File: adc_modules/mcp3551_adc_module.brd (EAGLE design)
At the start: 100 x 80 mm, 0 parts

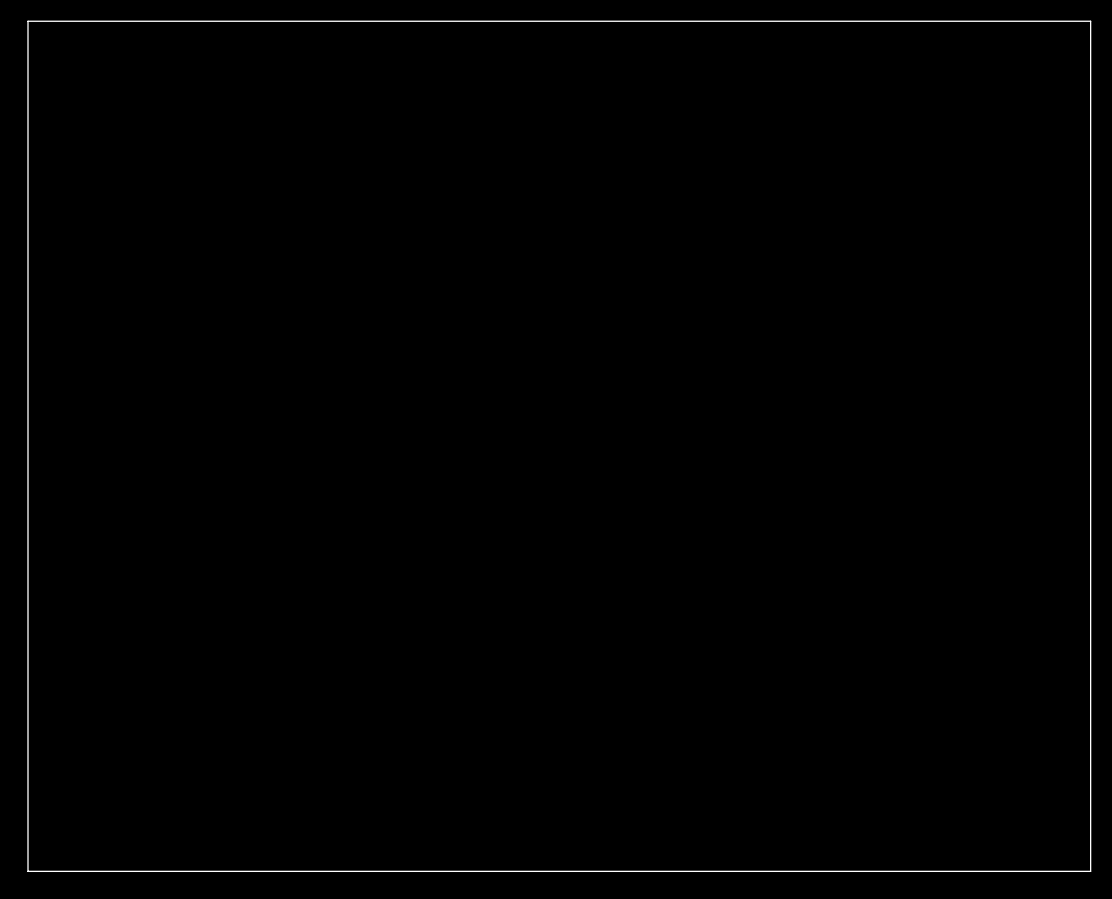
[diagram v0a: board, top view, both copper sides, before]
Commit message: * updated and almost finished MCP3551 ADC module
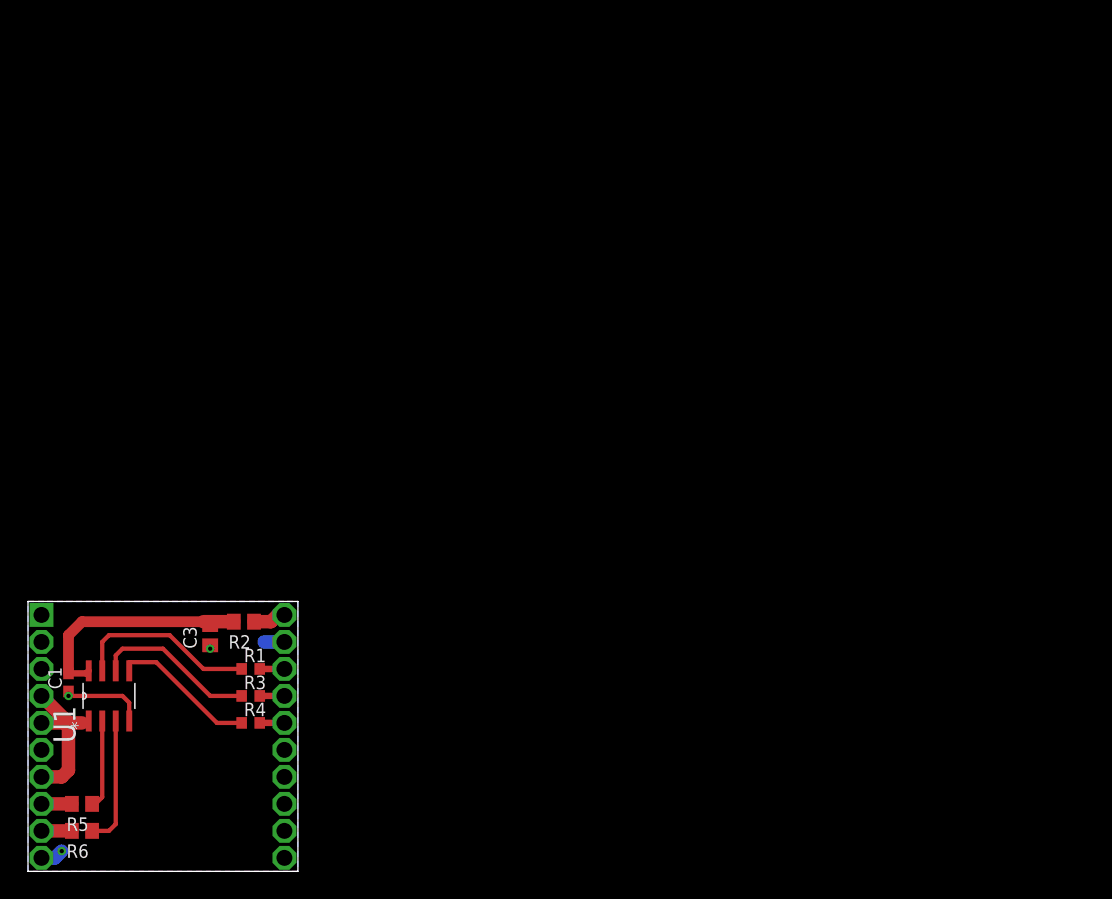
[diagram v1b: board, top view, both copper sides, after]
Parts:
- added C1: 100n, SquantorRCL:C0603
- added C3: 10u, SquantorRCL:C0805
- added R1, R3, R4: 100, SquantorRCL:R0603
- added R2: ferrite, SquantorRCL:R0805
- added R5, R6: 5.1k, SquantorRCL:R0805
- added U$1: METROLOGY_MODULE1.5MM, SquantorPCBOutline:METROLOGY_MODULE_1.5MM_HOLE
- added U1: MCP3553-E/SN, SquantorMicrochip:SOIC127P600X175-8N
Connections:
- new net ADC_CS: R1.1, U1.7
- new net ADC_SCK: R4.1, U1.5
- new net ADC_SDO: R3.1, U1.6
- new net ADC_VIN+: R5.1, U1.2
- new net ADC_VIN-: R6.1, U1.3
- new net GND: C1.1, C3.1, U$1.P$10, U$1.P$19, U$1.P$6, U1.4
- new net N$1: R2.1, U$1.P$20
- new net N$2: R1.2, U$1.P$18
- new net N$3: R3.2, U$1.P$17
- new net N$4: R4.2, U$1.P$16
- new net N$5: R5.2, U$1.P$8
- new net N$6: R6.2, U$1.P$9
- new net VCC: C1.2, C3.2, R2.2, U1.8
- new net VREF: U$1.P$4, U$1.P$5, U$1.P$7, U1.1
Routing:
- net VCC: track 0.00 -> 22.0 mm
- net ADC_CS: track 0.00 -> 17.4 mm
- net ADC_SDO: track 0.00 -> 15.4 mm
- net VREF: track 0.00 -> 15.4 mm
- net ADC_SCK: track 0.00 -> 13.8 mm
- net GND: track 0.00 -> 12.5 mm, vias 0 -> 3
- net ADC_VIN-: track 0.00 -> 12.2 mm
- net ADC_VIN+: track 0.00 -> 8.38 mm
- net N$1: track 0.00 -> 3.12 mm
- net N$6: track 0.00 -> 2.86 mm
- net N$5: track 0.00 -> 2.86 mm
- net N$4: track 0.00 -> 2.32 mm
- net N$3: track 0.00 -> 2.32 mm
- net N$2: track 0.00 -> 2.32 mm
- added copper zone on layer 16, net GND
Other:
- board size 100 x 80 mm -> 25.4 x 25.4 mm

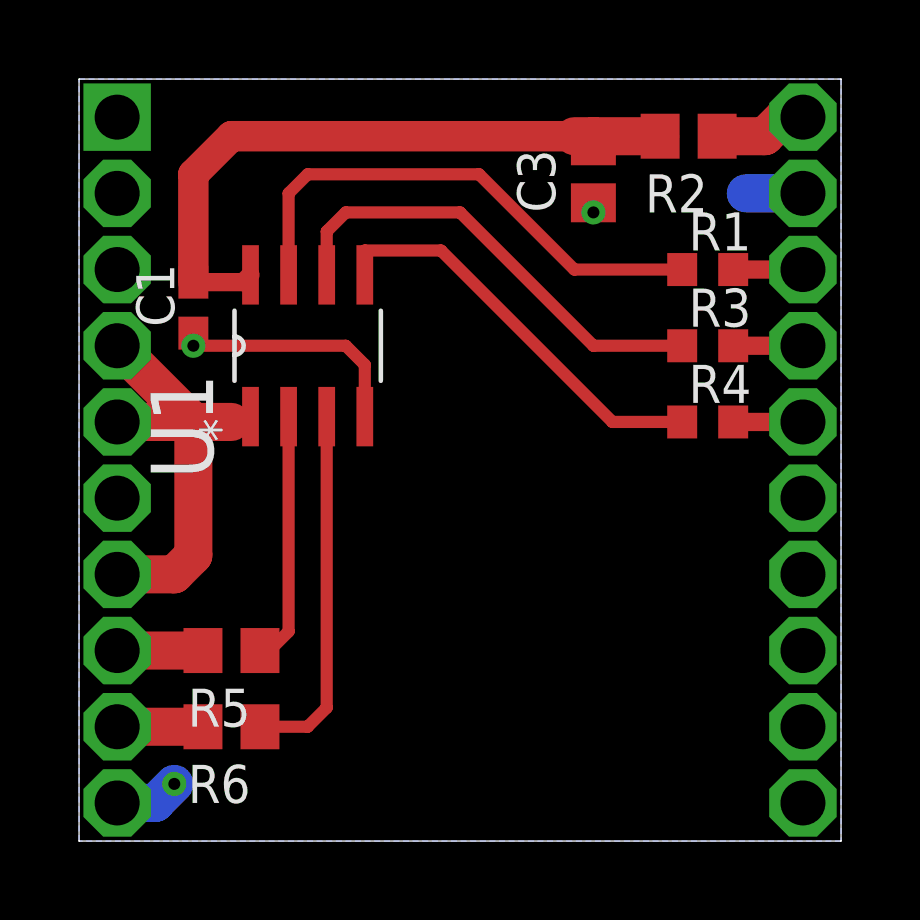
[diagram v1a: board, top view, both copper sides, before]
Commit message: * updated board format * made the LTC6655 reference module more compact, hopefully better * small modifications to the MCP355X ADC module
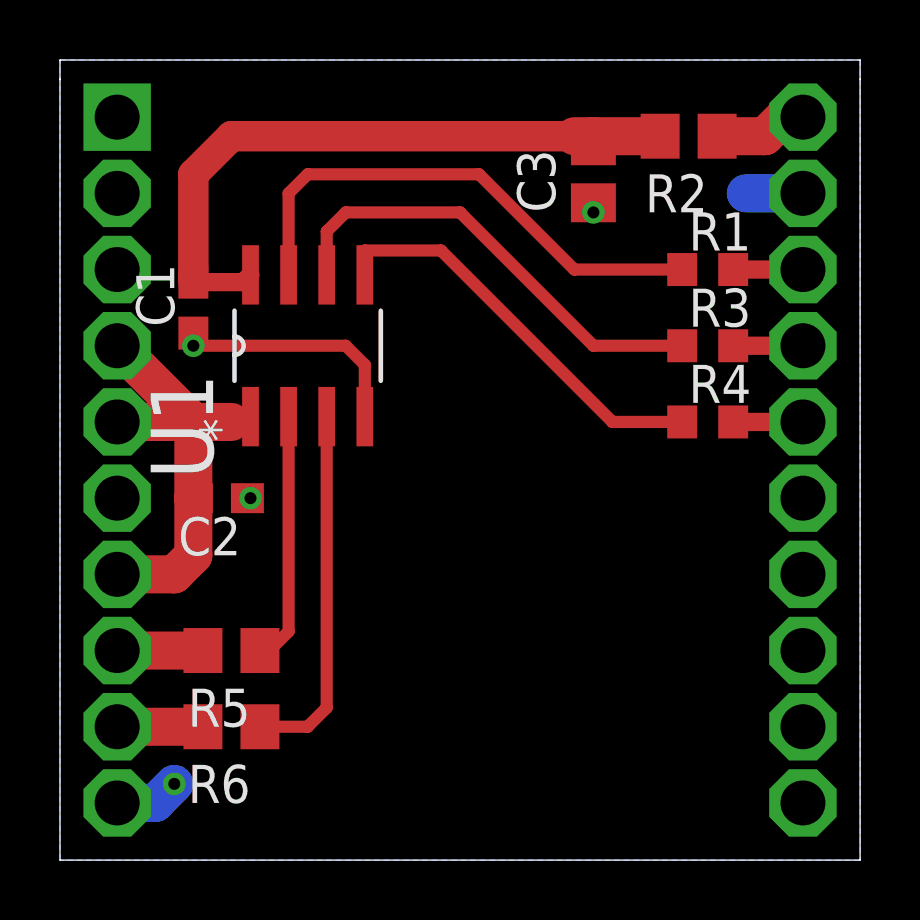
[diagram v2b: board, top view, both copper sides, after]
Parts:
- added C2: 100n, SquantorRCL:C0603
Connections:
- net GND: now also C2.1
- net VREF: now also C2.2
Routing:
- net GND: track 12.5 -> 12.6 mm, vias 3 -> 4
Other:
- board size 25.4 x 25.4 mm -> 26.7 x 26 mm
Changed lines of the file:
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@@
 <setting verticaltext="up"/>
 </settings>
-<grid distance="0.635" unitdist="mm" unit="mm" style="lines" multiple="1" display="yes" altdistance="0.025" altunitdist="inch" altunit="inch"/>
+<grid distance="12.5" unitdist="mil" unit="mm" style="lines" multiple="1" display="yes" altdistance="0.025" altunitdist="inch" altunit="inch"/>
 <layers>
 <layer number="1" name="Top" color="4" fill="1" visible="yes" active="yes"/>
@@
 <board>
 <plain>
-<wire x1="0" y1="25.4" x2="25.4" y2="25.4" width="0" layer="20"/>
+<wire x1="-0.635" y1="26.035" x2="26.035" y2="26.035" width="0" layer="20"/>
+<wire x1="-0.635" y1="25.4" x2="-0.635" y2="26.035" width="0" layer="20"/>
+<wire x1="26.035" y1="26.035" x2="26.035" y2="25.4" width="0" layer="20"/>
 </plain>
 <attributes>
@@
 </class>
 </classes>
-<designrules name="default">
+<designrules name="OSHPark">
 <description language="de">&lt;b&gt;EAGLE Design Rules&lt;/b&gt;
 &lt;p&gt;
@@
 Einstellungen hier und speichern die Design Rules unter
 einem neuen Namen ab.</description>
-<description language="en">&lt;b&gt;EAGLE Design Rules&lt;/b&gt;
+<description language="en">&lt;b&gt;Laen's PCB Order Design Rules&lt;/b&gt;
 &lt;p&gt;
-The default Design Rules have been set to cover
-a wide range of applications. Your particular design
-may have different requirements, so please make the
-necessary adjustments and save your customized
-design rules under a new name.</description>
+Please make sure your boards conform to these design rules.</description>
 <param name="layerSetup" value="(1*16)"/>
-<param name="mtCopper" value="0.035mm 0.035mm 0.035mm 0.035mm 0.035mm 0.035mm 0.035mm 0.035mm 0.035mm 0.035mm 0.035mm 0.035mm 0.035mm 0.035mm 0.035mm 0.035mm"/>
-<param name="mtIsolate" value="1.5mm 0.15mm 0.2mm 0.15mm 0.2mm 0.15mm 0.2mm 0.15mm 0.2mm 0.15mm 0.2mm 0.15mm 0.2mm 0.15mm 0.2mm"/>
-<param name="mdWireWire" value="8mil"/>
-<param name="mdWirePad" value="8mil"/>
-<param name="mdWireVia" value="8mil"/>
-<param name="mdPadPad" value="8mil"/>
-<param name="mdPadVia" value="8mil"/>
-<param name="mdViaVia" value="8mil"/>
-<param name="mdSmdPad" value="8mil"/>
-<param name="mdSmdVia" value="8mil"/>
-<param name="mdSmdSmd" value="8mil"/>
+<param name="mtCopper" value="0.0356mm 0.0356mm 0.0356mm 0.0356mm 0.0356mm 0.0356mm 0.0356mm 0.0356mm 0.0356mm 0.0356mm 0.0356mm 0.0356mm 0.0356mm 0.0356mm 0.0356mm 0.0356mm"/>
+<param name="mtIsolate" value="1.5011mm 0.1499mm 0.2007mm 0.1499mm 0.2007mm 0.1499mm 0.2007mm 0.1499mm 0.2007mm 0.1499mm 0.2007mm 0.1499mm 0.2007mm 0.1499mm 0.2007mm"/>
+<param name="mdWireWire" value="6mil"/>
+<param name="mdWirePad" value="6mil"/>
+<param name="mdWireVia" value="6mil"/>
+<param name="mdPadPad" value="6mil"/>
+<param name="mdPadVia" value="6mil"/>
+<param name="mdViaVia" value="6mil"/>
+<param name="mdSmdPad" value="6mil"/>
+<param name="mdSmdVia" value="6mil"/>
+<param name="mdSmdSmd" value="6mil"/>
 <param name="mdViaViaSameLayer" value="8mil"/>
 <param name="mnLayersViaInSmd" value="2"/>
-<param name="mdCopperDimension" value="40mil"/>
-<param name="mdDrill" value="8mil"/>
+<param name="mdCopperDimension" value="15mil"/>
+<param name="mdDrill" value="6mil"/>
 <param name="mdSmdStop" value="0mil"/>
-<param name="msWidth" value="10mil"/>
-<param name="msDrill" value="24mil"/>
-<param name="msMicroVia" value="9.99mm"/>
+<param name="msWidth" value="6mil"/>
+<param name="msDrill" value="13mil"/>
+<param name="msMicroVia" value="13mil"/>
 <param name="msBlindViaRatio" value="0.5"/>
 <param name="rvPadTop" value="0.25"/>
@@
 <param name="rvMicroViaOuter" value="0.25"/>
 <param name="rvMicroViaInner" value="0.25"/>
-<param name="rlMinPadTop" value="10mil"/>
+<param name="rlMinPadTop" value="7mil"/>
 <param name="rlMaxPadTop" value="20mil"/>
-<param name="rlMinPadInner" value="10mil"/>
+<param name="rlMinPadInner" value="7mil"/>
 <param name="rlMaxPadInner" value="20mil"/>
-<param name="rlMinPadBottom" value="10mil"/>
+<param name="rlMinPadBottom" value="7mil"/>
 <param name="rlMaxPadBottom" value="20mil"/>
-<param name="rlMinViaOuter" value="8mil"/>
+<param name="rlMinViaOuter" value="7mil"/>
 <param name="rlMaxViaOuter" value="20mil"/>
-<param name="rlMinViaInner" value="8mil"/>
+<param name="rlMinViaInner" value="7mil"/>
 <param name="rlMaxViaInner" value="20mil"/>
 <param name="rlMinMicroViaOuter" value="4mil"/>
@@
 <param name="mvStopFrame" value="1"/>
 <param name="mvCreamFrame" value="0"/>
-<param name="mlMinStopFrame" value="4mil"/>
-<param name="mlMaxStopFrame" value="4mil"/>
+<param name="mlMinStopFrame" value="3mil"/>
+<param name="mlMaxStopFrame" value="3mil"/>
 <param name="mlMinCreamFrame" value="0mil"/>
 <param name="mlMaxCreamFrame" value="0mil"/>
@@
 <element name="R5" library="SquantorRCL" package="R0805" value="5.1k" x="5.08" y="6.35" rot="R180"/>
 <element name="R6" library="SquantorRCL" package="R0805" value="5.1k" x="5.08" y="3.81" rot="R180"/>
+<element name="C2" library="SquantorRCL" package="C0603" value="100n" x="4.7625" y="11.43" rot="R180"/>
 </elements>
 <signals>
@@
 <contactref element="C1" pad="1"/>
 <polygon width="0.8128" layer="16" isolate="0.4064">
-<vertex x="0" y="25.4"/>
-<vertex x="25.4" y="25.4"/>
-<vertex x="25.4" y="0"/>
-<vertex x="0" y="0"/>
+<vertex x="-0.635" y="26.035"/>
+<vertex x="26.035" y="26.035"/>
+<vertex x="26.035" y="-0.635"/>
+<vertex x="-0.635" y="-0.635"/>
 </polygon>
 <contactref element="U$1" pad="P$6"/>
@@
 <wire x1="2.54" y1="1.27" x2="3.175" y2="1.905" width="1.27" layer="16"/>
 <wire x1="17.145" y1="21.275" x2="17.145" y2="20.955" width="0.4064" layer="1"/>
+<contactref element="C2" pad="1"/>
+<via x="5.715" y="11.43" extent="1-16" drill="0.4" shape="octagon"/>
+<wire x1="5.6125" y1="11.43" x2="5.715" y2="11.43" width="0.4064" layer="1"/>
 </signal>
 <signal name="N$1">
@@
 <wire x1="1.27" y1="8.89" x2="3.175" y2="8.89" width="1.27" layer="1"/>
 <wire x1="3.175" y1="8.89" x2="3.81" y2="9.525" width="1.27" layer="1"/>
-<wire x1="3.81" y1="9.525" x2="3.81" y2="13.97" width="1.27" layer="1"/>
+<wire x1="3.81" y1="9.525" x2="3.81" y2="11.43" width="1.27" layer="1"/>
+<contactref element="C2" pad="2"/>
+<wire x1="3.81" y1="11.43" x2="3.81" y2="13.97" width="1.27" layer="1"/>
+<wire x1="3.9125" y1="11.43" x2="3.81" y2="11.43" width="0.4064" layer="1"/>
 </signal>
 <signal name="ADC_VIN-">
@@
 </signal>
 </signals>
+<errors>
+</errors>
 </board>
 </drawing>

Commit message: * modified boards and processed for production
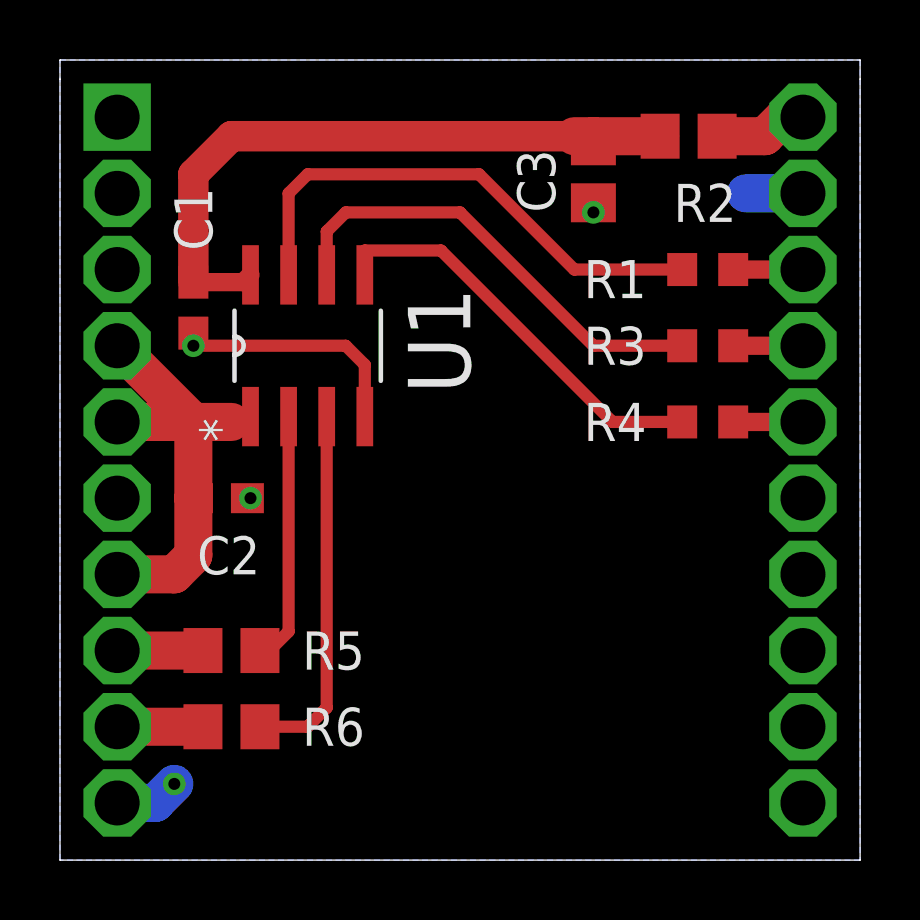
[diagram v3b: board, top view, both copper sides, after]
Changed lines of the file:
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@@
 </autorouter>
 <elements>
-<element name="R2" library="SquantorRCL" package="R0805" value="ferrite" x="20.32" y="23.495" rot="R180"/>
-<element name="C3" library="SquantorRCL" package="C0805" value="10u" x="17.145" y="22.225" rot="R90"/>
+<element name="R2" library="SquantorRCL" package="R0805" value="ferrite" x="20.32" y="23.495" smashed="yes" rot="R180">
+<attribute name="NAME" x="21.9075" y="21.9075" size="1.27" layer="25" rot="R180"/>
+</element>
+<element name="C3" library="SquantorRCL" package="C0805" value="10u" x="17.145" y="22.225" smashed="yes" rot="R90">
+<attribute name="NAME" x="15.875" y="20.955" size="1.27" layer="25" rot="R90"/>
+</element>
 <element name="U$1" library="SquantorPCBOutline" package="METROLOGY_MODULE_1.5MM_HOLE" value="METROLOGY_MODULE1.5MM" x="12.7" y="12.7"/>
-<element name="U1" library="SquantorMicrochip" package="SOIC127P600X175-8N" value="MCP3553-E/SN" x="7.62" y="16.51" rot="R90">
+<element name="U1" library="SquantorMicrochip" package="SOIC127P600X175-8N" value="MCP3553-E/SN" x="7.62" y="16.51" smashed="yes" rot="R90">
 <attribute name="PACKAGE" value="SOIC-8" x="7.62" y="16.51" size="1.778" layer="27" rot="R90" display="off"/>
 <attribute name="OC_NEWARK" value="56K7004" x="7.62" y="16.51" size="1.778" layer="27" rot="R90" display="off"/>
@@
 <attribute name="OC_FARNELL" value="1605569" x="7.62" y="16.51" size="1.778" layer="27" rot="R90" display="off"/>
 <attribute name="MPN" value="MCP3553-E/SN" x="7.62" y="16.51" size="1.778" layer="27" rot="R90" display="off"/>
+<attribute name="NAME" x="13.0429" y="14.9225" size="2.0828" layer="25" ratio="10" rot="SR90"/>
 </element>
-<element name="C1" library="SquantorRCL" package="C0603" value="100n" x="3.81" y="17.78" rot="R90"/>
-<element name="R1" library="SquantorRCL" package="R0603" value="100" x="20.955" y="19.05"/>
-<element name="R3" library="SquantorRCL" package="R0603" value="100" x="20.955" y="16.51"/>
-<element name="R4" library="SquantorRCL" package="R0603" value="100" x="20.955" y="13.97"/>
-<element name="R5" library="SquantorRCL" package="R0805" value="5.1k" x="5.08" y="6.35" rot="R180"/>
-<element name="R6" library="SquantorRCL" package="R0805" value="5.1k" x="5.08" y="3.81" rot="R180"/>
-<element name="C2" library="SquantorRCL" package="C0603" value="100n" x="4.7625" y="11.43" rot="R180"/>
+<element name="C1" library="SquantorRCL" package="C0603" value="100n" x="3.81" y="17.78" smashed="yes" rot="R90">
+<attribute name="NAME" x="4.445" y="19.685" size="1.27" layer="25" rot="R90"/>
+</element>
+<element name="R1" library="SquantorRCL" package="R0603" value="100" x="20.955" y="19.05" smashed="yes">
+<attribute name="NAME" x="16.8275" y="18.0975" size="1.27" layer="25"/>
+</element>
+<element name="R3" library="SquantorRCL" package="R0603" value="100" x="20.955" y="16.51" smashed="yes">
+<attribute name="NAME" x="16.8275" y="15.875" size="1.27" layer="25"/>
+</element>
+<element name="R4" library="SquantorRCL" package="R0603" value="100" x="20.955" y="13.97" smashed="yes">
+<attribute name="NAME" x="16.8275" y="13.335" size="1.27" layer="25"/>
+</element>
+<element name="R5" library="SquantorRCL" package="R0805" value="5.1k" x="5.08" y="6.35" smashed="yes" rot="R180">
+<attribute name="NAME" x="9.525" y="6.985" size="1.27" layer="25" rot="R180"/>
+</element>
+<element name="R6" library="SquantorRCL" package="R0805" value="5.1k" x="5.08" y="3.81" smashed="yes" rot="R180">
+<attribute name="NAME" x="9.525" y="4.445" size="1.27" layer="25" rot="R180"/>
+</element>
+<element name="C2" library="SquantorRCL" package="C0603" value="100n" x="4.7625" y="11.43" smashed="yes" rot="R180">
+<attribute name="NAME" x="6.0325" y="10.16" size="1.27" layer="25" rot="R180"/>
+</element>
 </elements>
 <signals>
